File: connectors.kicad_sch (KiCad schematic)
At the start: 4 parts, among them J1 Conn_01x04_Pin, J2 Conn_01x04_Pin, J3 Conn_01x09_Pin, J4 Conn_02x03_Odd_Even

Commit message: added footprints
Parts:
- J1, J2: footprint (none) -> Connector_PinHeader_2.54mm:PinHeader_1x04_P2.54mm_Vertical
- J3: footprint (none) -> Connector_PinHeader_2.54mm:PinHeader_1x09_P2.54mm_Vertical
- J4: footprint (none) -> Connector_PinHeader_2.54mm:PinHeader_2x03_P2.54mm_Vertical
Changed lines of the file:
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@@
 			)
 		)
-		(property "Footprint" ""
+		(property "Footprint" "Connector_PinHeader_2.54mm:PinHeader_1x09_P2.54mm_Vertical"
 			(at 185.42 116.84 0)
 			(effects
@@
 			)
 		)
-		(property "Footprint" ""
+		(property "Footprint" "Connector_PinHeader_2.54mm:PinHeader_1x04_P2.54mm_Vertical"
 			(at 152.4 116.84 0)
 			(effects
@@
 			)
 		)
-		(property "Footprint" ""
+		(property "Footprint" "Connector_PinHeader_2.54mm:PinHeader_1x04_P2.54mm_Vertical"
 			(at 129.54 116.84 0)
 			(effects
@@
 			)
 		)
-		(property "Footprint" ""
+		(property "Footprint" "Connector_PinHeader_2.54mm:PinHeader_2x03_P2.54mm_Vertical"
 			(at 215.9 116.84 0)
 			(effects

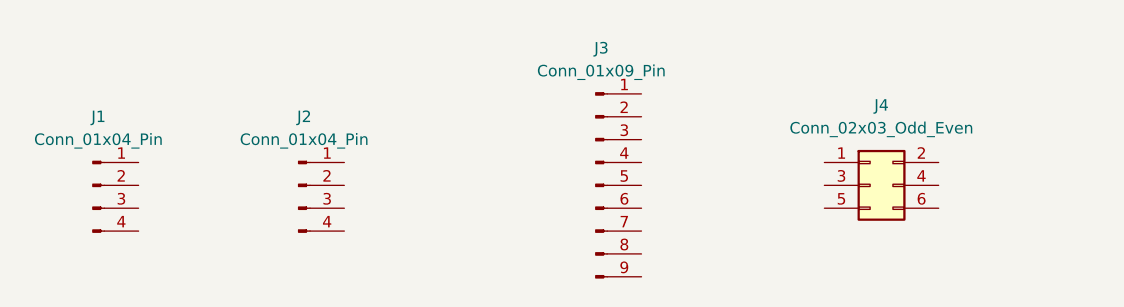
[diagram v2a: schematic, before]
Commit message: wired the components
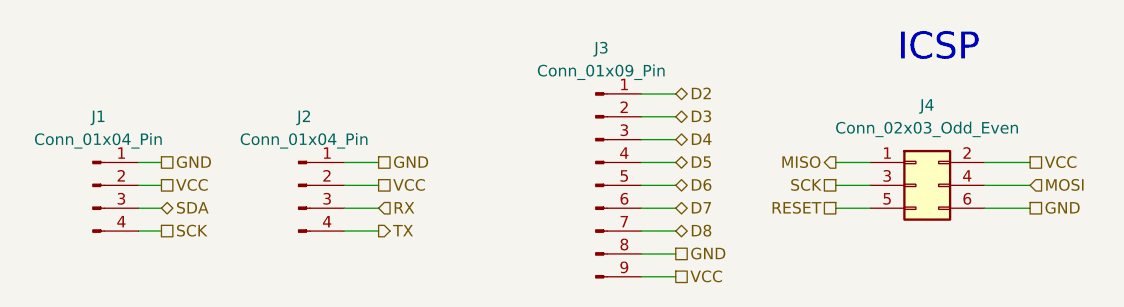
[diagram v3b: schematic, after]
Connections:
- net D2: now reaches J3.1 (Pin_1)
- net D3: now reaches J3.2 (Pin_2)
- net D4: now reaches J3.3 (Pin_3)
- net D5: now reaches J3.4 (Pin_4)
- net D6: now reaches J3.5 (Pin_5)
- net D7: now reaches J3.6 (Pin_6)
- net D8: now reaches J3.7 (Pin_7)
- net GND: now reaches J3.8 (Pin_8)
- net GND: now also J1.1 (Pin_1), J2.1 (Pin_1), J4.6 (Pin_6)
- net VCC: now reaches J3.9 (Pin_9)
- net VCC: now also J1.2 (Pin_2), J2.2 (Pin_2), J4.2 (Pin_2)
- net RX: now reaches J2.3 (Pin_3)
- net TX: now reaches J2.4 (Pin_4)
- net SDA: now reaches J1.3 (Pin_3)
- net SCK: now reaches J1.4 (Pin_4)
- net SCK: now also J4.3 (Pin_3)
- net MISO: now reaches J4.1 (Pin_1)
- net MOSI: now reaches J4.4 (Pin_4)
- net RESET: now reaches J4.5 (Pin_5)
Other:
- note added: "ICSP"
- moved on the sheet: J4

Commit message: changed layout
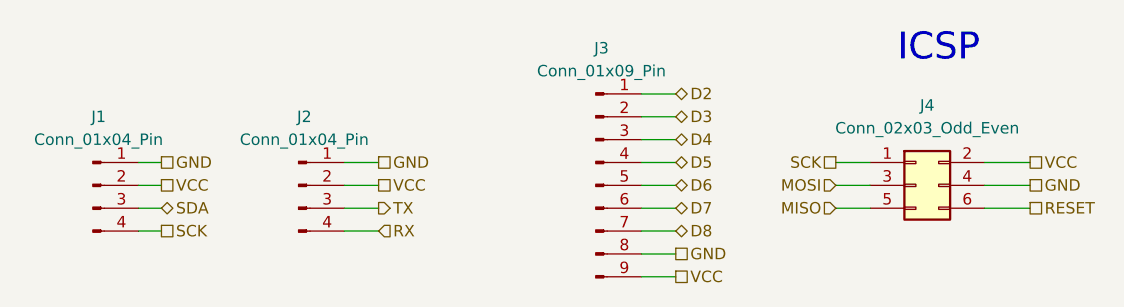
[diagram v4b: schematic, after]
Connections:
- net GND: now also J4.4 (Pin_4); no longer J4.6 (Pin_6)
- net MISO: now also J4.5 (Pin_5); no longer J4.1 (Pin_1)
- net MOSI: now also J4.3 (Pin_3); no longer J4.4 (Pin_4)
- net RESET: now also J4.6 (Pin_6); no longer J4.5 (Pin_5)
- net RX: now also J2.4 (Pin_4); no longer J2.3 (Pin_3)
- net SCK: now also J4.1 (Pin_1); no longer J4.3 (Pin_3)
- net TX: now also J2.3 (Pin_3); no longer J2.4 (Pin_4)
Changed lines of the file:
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@@
 		)
 	)
-	(hierarchical_label "SCK"
-		(shape passive)
+	(hierarchical_label "MOSI"
+		(shape input)
 		(at 212.09 116.84 180)
 		(effects
@@
 		)
 	)
-	(hierarchical_label "MISO"
-		(shape output)
+	(hierarchical_label "SCK"
+		(shape passive)
 		(at 212.09 114.3 180)
 		(effects
@@
 		)
 	)
-	(hierarchical_label "GND"
+	(hierarchical_label "RESET"
 		(shape passive)
 		(at 233.68 119.38 0)
@@
 		)
 	)
-	(hierarchical_label "RESET"
-		(shape passive)
+	(hierarchical_label "MISO"
+		(shape input)
 		(at 212.09 119.38 180)
 		(effects
@@
 		)
 	)
-	(hierarchical_label "MOSI"
-		(shape input)
+	(hierarchical_label "GND"
+		(shape passive)
 		(at 233.68 116.84 0)
 		(effects
@@
 		)
 	)
-	(hierarchical_label "RX"
-		(shape input)
+	(hierarchical_label "TX"
+		(shape output)
 		(at 161.29 119.38 0)
 		(effects
@@
 		)
 	)
-	(hierarchical_label "TX"
-		(shape output)
+	(hierarchical_label "RX"
+		(shape input)
 		(at 161.29 121.92 0)
 		(effects
